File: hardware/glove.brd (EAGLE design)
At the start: 50.8 x 36.8 mm, 84 parts, among them J1 TC2030-JLINK-NL, J2 MICRO_USB_B_JST_MC5BR3-M404-4S, P1 DMP1045U, U1 NRF51822QF, U2 BNO055, U3 AT42QT1070, U4 MCP73831, U5 LP3855EMP-ADJ, X1 ABS05-32.768KHZ-9-T

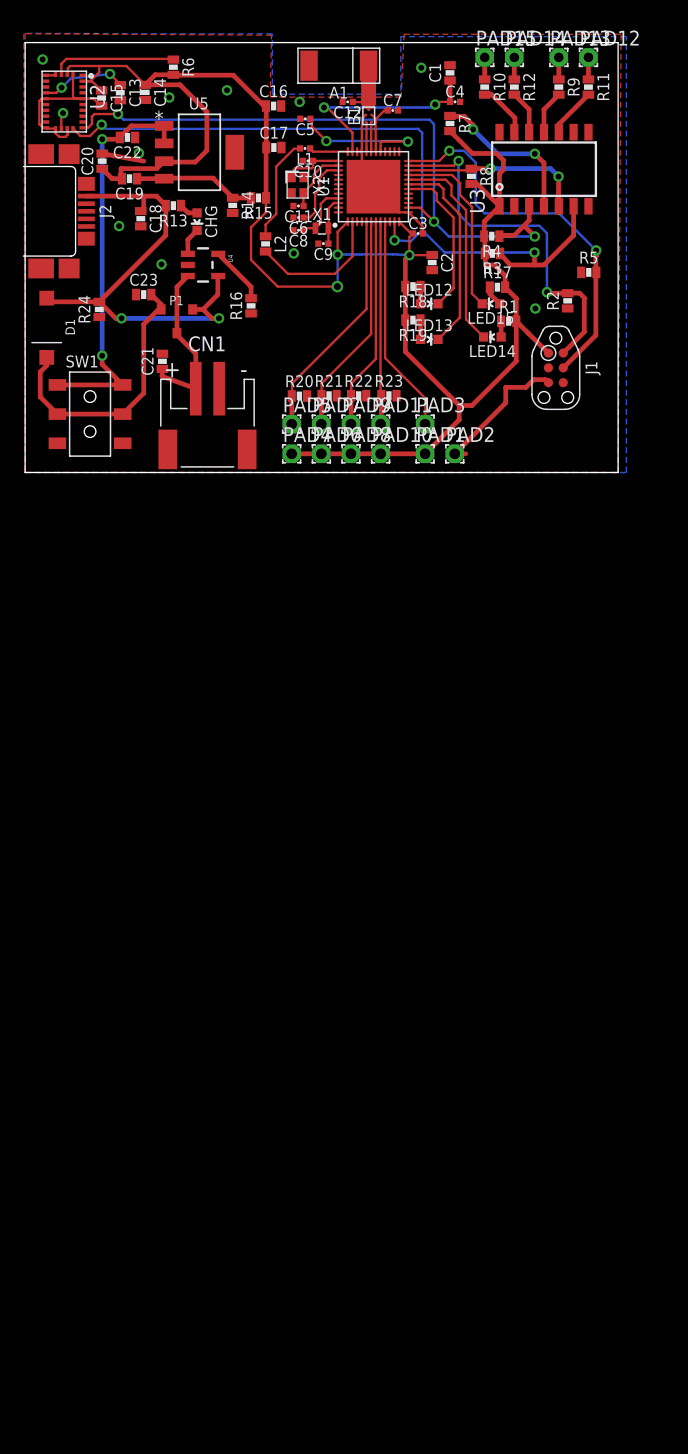
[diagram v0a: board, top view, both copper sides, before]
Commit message: Silkscreen/SPI LEDs
Cleaned up silk screen layer.
Added SPI connectors to schematic - still need to route.
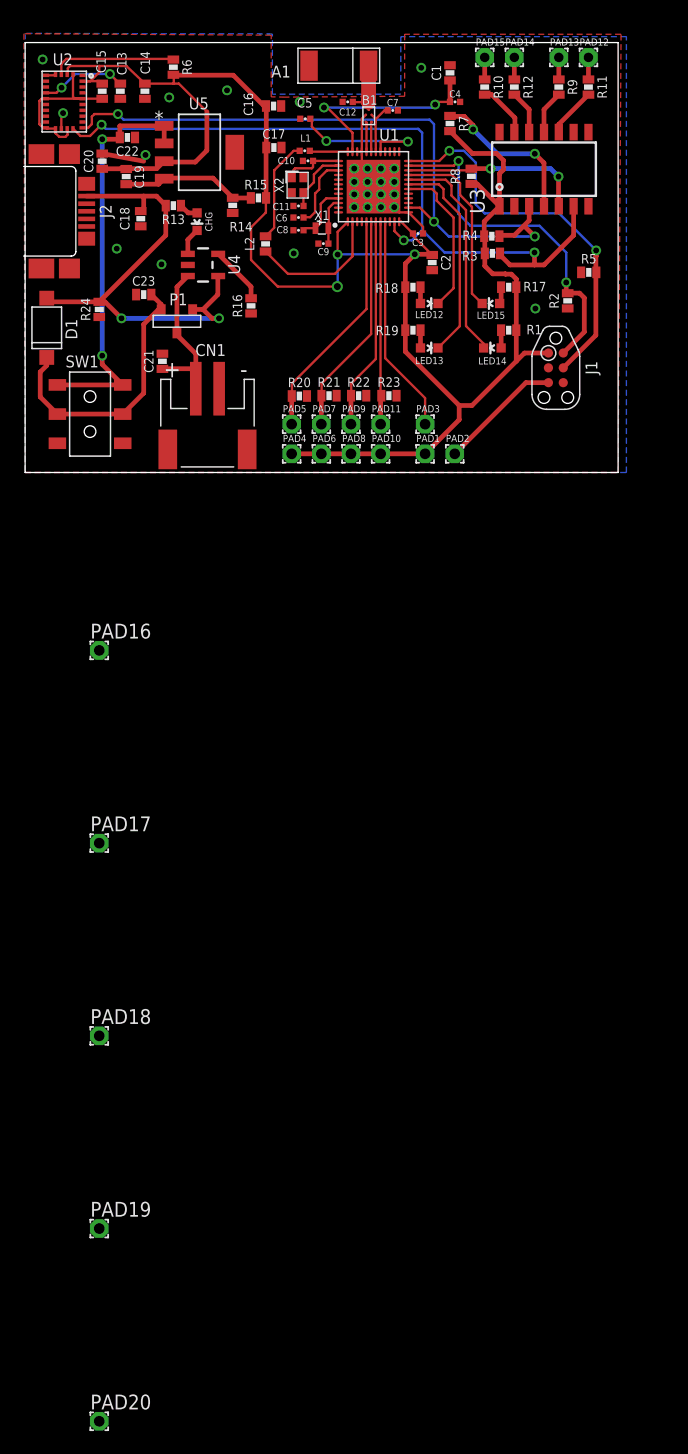
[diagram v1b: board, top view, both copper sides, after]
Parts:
- added PAD16, PAD17, PAD18, PAD19, PAD20: WIREPAD1,6/0,9, wirepad:1,6/0,9
- moved R17 0.97 mm to (41.4, 10.8)
- moved LED14 0.94 mm to (40.0, 5.59)
- moved R19 0.86 mm to (33.2, 7.11)
- moved R1 0.76 mm to (41.4, 7.11)
- moved LED13 0.74 mm to (34.6, 5.59)
- moved C15 0.59 mm to (6.60, 27.6)
- moved C19 0.33 mm to (8.66, 20.3), turned to 90 degrees
- moved L1 0.20 mm to (24.0, 22.5)
- moved C13 0.13 mm to (8.15, 27.6)
- moved C14 0.10 mm to (10.3, 27.6)
- moved R18 0.05 mm to (33.2, 10.8)
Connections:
- new net MISO: PAD19.1, U1.4
- new net MOSI: PAD20.1, U1.3
- new net SCLK: PAD18.1, U1.10
- net GND: now also PAD17.1
- net VCC: now also PAD16.1
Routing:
- net GND: track 45.7 -> 42.2 mm, vias 11 -> 27
- net VCC: track 154.9 -> 152.4 mm
- net N$7: track 10.5 -> 11.6 mm
- net N$19: track 31.2 -> 30.2 mm
- net N$6: track 18.0 -> 18.9 mm
- net N$41: track 14.5 -> 13.6 mm
- net N$43: track 17.4 -> 18.1 mm
- net N$5: track 34.9 -> 35.5 mm

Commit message: Added SPI LEDs to board
Need to fix clearance
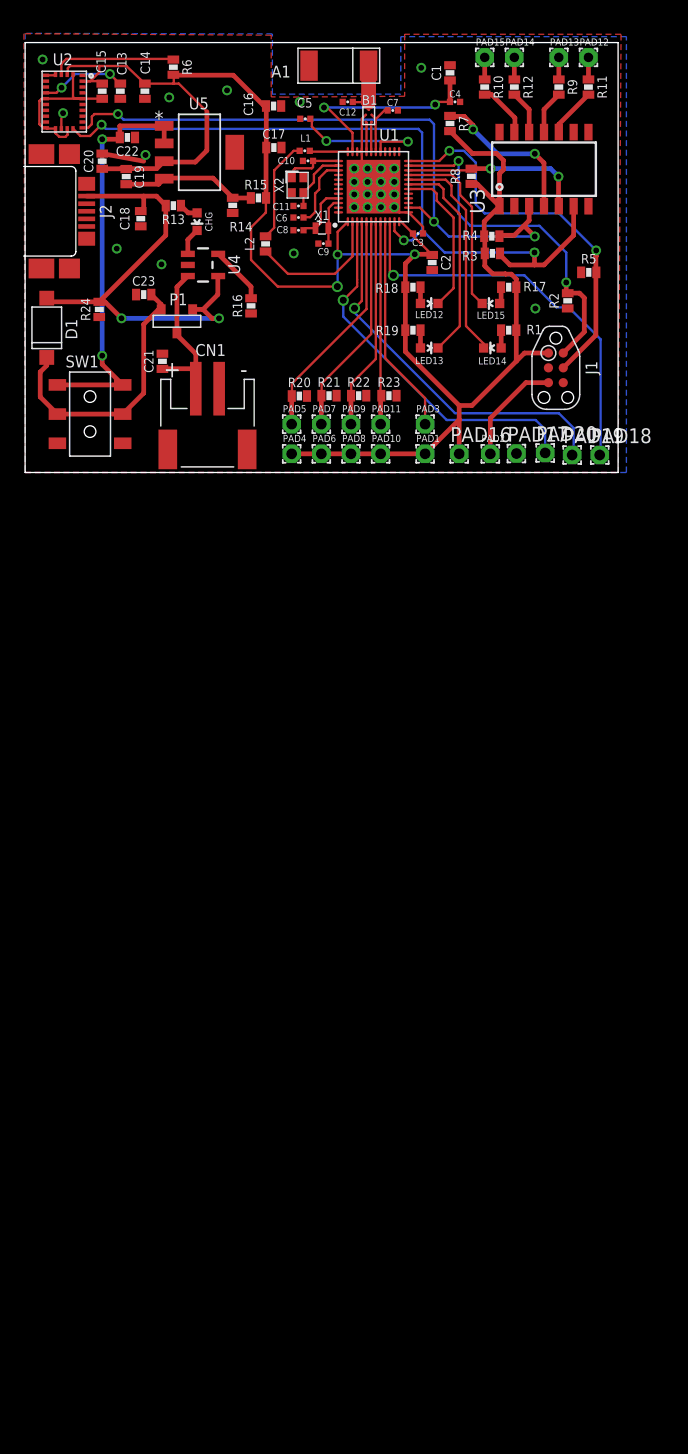
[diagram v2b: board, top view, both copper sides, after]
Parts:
- moved PAD20 91.3 mm to (44.6, -3.40)
- moved PAD19 77.7 mm to (46.9, -3.58)
- moved PAD18 65.7 mm to (49.2, -3.58)
- moved PAD17 48.9 mm to (42.1, -3.45)
- moved PAD16 35.1 mm to (37.2, -3.48)
- moved PAD2 3.05 mm to (39.9, -3.48)
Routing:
- net SCLK: track 0.00 -> 34.7 mm, vias 0 -> 1
- net MISO: track 0.00 -> 33.3 mm, vias 0 -> 1
- net MOSI: track 0.00 -> 31.9 mm, vias 0 -> 1
- net VCC: track 152.4 -> 155.5 mm
- net GND: track 42.2 -> 40.9 mm
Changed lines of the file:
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@@
 <?xml version="1.0" encoding="utf-8"?>
 <!DOCTYPE eagle SYSTEM "eagle.dtd">
-<eagle version="7.7.0">
+<eagle version="7.6.0">
 <drawing>
 <settings>
@@
 <attribute name="VALUE" x="30.4546" y="-0.3398" size="0.0254" layer="27"/>
 </element>
-<element name="PAD2" library="wirepad" package="1,6/0,9" value="WIREPAD1,6/0,9" x="36.8046" y="-3.4798" smashed="yes">
-<attribute name="NAME" x="36.0426" y="-2.4638" size="0.6096" layer="25" ratio="10"/>
-<attribute name="VALUE" x="36.8046" y="-2.8798" size="0.0254" layer="27"/>
+<element name="PAD2" library="wirepad" package="1,6/0,9" value="WIREPAD1,6/0,9" x="39.8526" y="-3.4798" smashed="yes">
+<attribute name="NAME" x="39.0906" y="-2.4638" size="0.6096" layer="25" ratio="10"/>
+<attribute name="VALUE" x="39.8526" y="-2.8798" size="0.0254" layer="27"/>
 </element>
 <element name="PAD3" library="wirepad" package="1,6/0,9" value="WIREPAD1,6/0,9" x="34.2646" y="-0.9398" smashed="yes">
@@
 <attribute name="VALUE" x="-1.3208" y="11.1252" size="1.27" layer="27" rot="R270"/>
 </element>
-<element name="PAD16" library="wirepad" package="1,6/0,9" value="WIREPAD1,6/0,9" x="6.35" y="-20.32"/>
-<element name="PAD17" library="wirepad" package="1,6/0,9" value="WIREPAD1,6/0,9" x="6.35" y="-36.83"/>
-<element name="PAD18" library="wirepad" package="1,6/0,9" value="WIREPAD1,6/0,9" x="6.35" y="-53.34"/>
-<element name="PAD19" library="wirepad" package="1,6/0,9" value="WIREPAD1,6/0,9" x="6.35" y="-69.85"/>
-<element name="PAD20" library="wirepad" package="1,6/0,9" value="WIREPAD1,6/0,9" x="6.35" y="-86.36"/>
+<element name="PAD16" library="wirepad" package="1,6/0,9" value="WIREPAD1,6/0,9" x="37.1856" y="-3.4798"/>
+<element name="PAD17" library="wirepad" package="1,6/0,9" value="WIREPAD1,6/0,9" x="42.0878" y="-3.4544"/>
+<element name="PAD18" library="wirepad" package="1,6/0,9" value="WIREPAD1,6/0,9" x="49.2252" y="-3.5814"/>
+<element name="PAD19" library="wirepad" package="1,6/0,9" value="WIREPAD1,6/0,9" x="46.863" y="-3.5814"/>
+<element name="PAD20" library="wirepad" package="1,6/0,9" value="WIREPAD1,6/0,9" x="44.5516" y="-3.4036"/>
 </elements>
 <signals>
@@
 <via x="33.9344" y="29.591" extent="1-16" drill="0.5"/>
 <via x="43.7134" y="8.9662" extent="1-16" drill="0.5"/>
-<wire x1="36.8046" y1="-3.4798" x2="42.9006" y2="2.6162" width="0.4064" layer="1"/>
 <wire x1="42.9006" y1="2.6162" x2="44.831" y2="2.6162" width="0.4064" layer="1"/>
 <via x="28.194" y="20.955" extent="1-16" drill="0.5"/>
@@
 <contactref element="PAD17" pad="1"/>
 <wire x1="6.593" y1="26.9454" x2="6.604" y2="26.9344" width="0.2032" layer="1"/>
-<wire x1="16.621" y1="2.0998" x2="6.35" y2="-36.83" width="0" layer="19" extent="1-1"/>
+<wire x1="39.8526" y1="-3.4798" x2="39.8526" y2="-0.4318" width="0.4064" layer="1"/>
+<wire x1="39.8526" y1="-0.4318" x2="42.9006" y2="2.6162" width="0.4064" layer="1"/>
 </signal>
 <signal name="N$14">
@@
 <wire x1="32.5732" y1="12.812" x2="33.3756" y2="13.6144" width="0.4064" layer="1"/>
 <contactref element="PAD16" pad="1"/>
-<wire x1="8.2146" y1="20.955" x2="11.2776" y2="20.955" width="0.4064" layer="1"/>
+<wire x1="8.2146" y1="20.955" x2="8.89" y2="20.955" width="0.4064" layer="1"/>
+<wire x1="8.89" y1="20.955" x2="11.2776" y2="20.955" width="0.4064" layer="1"/>
 <wire x1="11.2776" y1="20.955" x2="11.9126" y2="21.59" width="0.4064" layer="1"/>
 <wire x1="6.604" y1="20.94" x2="8.6406" y2="20.94" width="0.4064" layer="1"/>
@@
 <wire x1="40.0558" y1="11.938" x2="41.133" y2="11.938" width="0.4064" layer="1"/>
 <wire x1="41.133" y1="11.938" x2="41.1584" y2="11.9126" width="0.4064" layer="1"/>
-<wire x1="8.2146" y1="20.955" x2="8.6406" y2="20.94" width="0" layer="19" extent="1-1"/>
-<wire x1="6.35" y1="-20.32" x2="22.6314" y2="-3.4798" width="0" layer="19" extent="1-1"/>
+<wire x1="37.1856" y1="-3.4798" x2="37.1856" y2="-0.5588" width="0.4064" layer="1"/>
+<wire x1="8.6406" y1="20.94" x2="8.875" y2="20.94" width="0.2032" layer="1"/>
+<wire x1="8.875" y1="20.94" x2="8.89" y2="20.955" width="0.2032" layer="1"/>
 </signal>
 <signal name="N$19">
@@
 <contactref element="U1" pad="4"/>
 <contactref element="PAD19" pad="1"/>
-<wire x1="28.845" y1="16.4056" x2="6.35" y2="-69.85" width="0" layer="19" extent="1-1"/>
+<wire x1="28.845" y1="16.4056" x2="28.845" y2="9.6172" width="0.2032" layer="1"/>
+<wire x1="28.845" y1="9.6172" x2="28.2194" y2="8.9916" width="0.2032" layer="1"/>
+<via x="28.2194" y="8.9916" extent="1-16" drill="0.6"/>
+<wire x1="28.2194" y1="8.9916" x2="28.2194" y2="8.6106" width="0.2032" layer="16"/>
+<wire x1="28.2194" y1="8.6106" x2="36.83" y2="0" width="0.2032" layer="16"/>
+<wire x1="36.83" y1="0" x2="45.72" y2="0" width="0.2032" layer="16"/>
+<wire x1="45.72" y1="0" x2="46.99" y2="-1.27" width="0.2032" layer="16"/>
+<wire x1="46.99" y1="-1.27" x2="46.99" y2="-3.4544" width="0.2032" layer="16"/>
+<wire x1="46.863" y1="-3.5814" x2="46.99" y2="-3.4544" width="0.2032" layer="16"/>
 </signal>
 <signal name="MOSI">
 <contactref element="U1" pad="3"/>
 <contactref element="PAD20" pad="1"/>
-<wire x1="28.445" y1="16.4056" x2="6.35" y2="-86.36" width="0" layer="19" extent="1-1"/>
+<wire x1="28.445" y1="16.4056" x2="28.445" y2="11.43" width="0.2032" layer="1"/>
+<wire x1="28.445" y1="11.43" x2="28.445" y2="11.173" width="0.2032" layer="1"/>
+<wire x1="27.2542" y1="9.6774" x2="27.2542" y2="8.2804" width="0.2032" layer="16"/>
+<wire x1="27.2542" y1="8.2804" x2="36.1188" y2="-0.5842" width="0.2032" layer="16"/>
+<wire x1="36.1188" y1="-0.5842" x2="43.7388" y2="-0.5842" width="0.2032" layer="16"/>
+<wire x1="43.7388" y1="-0.5842" x2="44.5516" y2="-1.397" width="0.2032" layer="16"/>
+<via x="27.2542" y="9.6774" extent="1-16" drill="0.6"/>
+<wire x1="27.2542" y1="9.6774" x2="28.445" y2="10.8682" width="0.2032" layer="1"/>
+<wire x1="28.445" y1="10.8682" x2="28.445" y2="11.173" width="0.2032" layer="1"/>
+<wire x1="44.5516" y1="-3.4036" x2="44.5516" y2="-1.397" width="0.2032" layer="16"/>
 </signal>
 <signal name="SCLK">
 <contactref element="U1" pad="10"/>
 <contactref element="PAD18" pad="1"/>
-<wire x1="31.245" y1="16.4056" x2="6.35" y2="-53.34" width="0" layer="19" extent="1-1"/>
+<wire x1="31.245" y1="16.4056" x2="31.245" y2="12.1128" width="0.2032" layer="1"/>
+<wire x1="31.245" y1="12.1128" x2="31.5468" y2="11.811" width="0.2032" layer="1"/>
+<via x="31.5468" y="11.811" extent="1-16" drill="0.6"/>
+<wire x1="31.5468" y1="11.811" x2="42.7736" y2="11.811" width="0.2032" layer="16"/>
+<wire x1="42.7736" y1="11.811" x2="45.5168" y2="9.0678" width="0.2032" layer="16"/>
+<wire x1="45.5168" y1="9.0678" x2="46.5582" y2="9.0678" width="0.2032" layer="16"/>
+<wire x1="46.5582" y1="9.0678" x2="49.3014" y2="6.3246" width="0.2032" layer="16"/>
+<wire x1="49.3014" y1="6.3246" x2="49.3014" y2="-3.5052" width="0.2032" layer="16"/>
+<wire x1="49.3014" y1="-3.5052" x2="49.2252" y2="-3.5814" width="0.2032" layer="16"/>
 </signal>
 </signals>

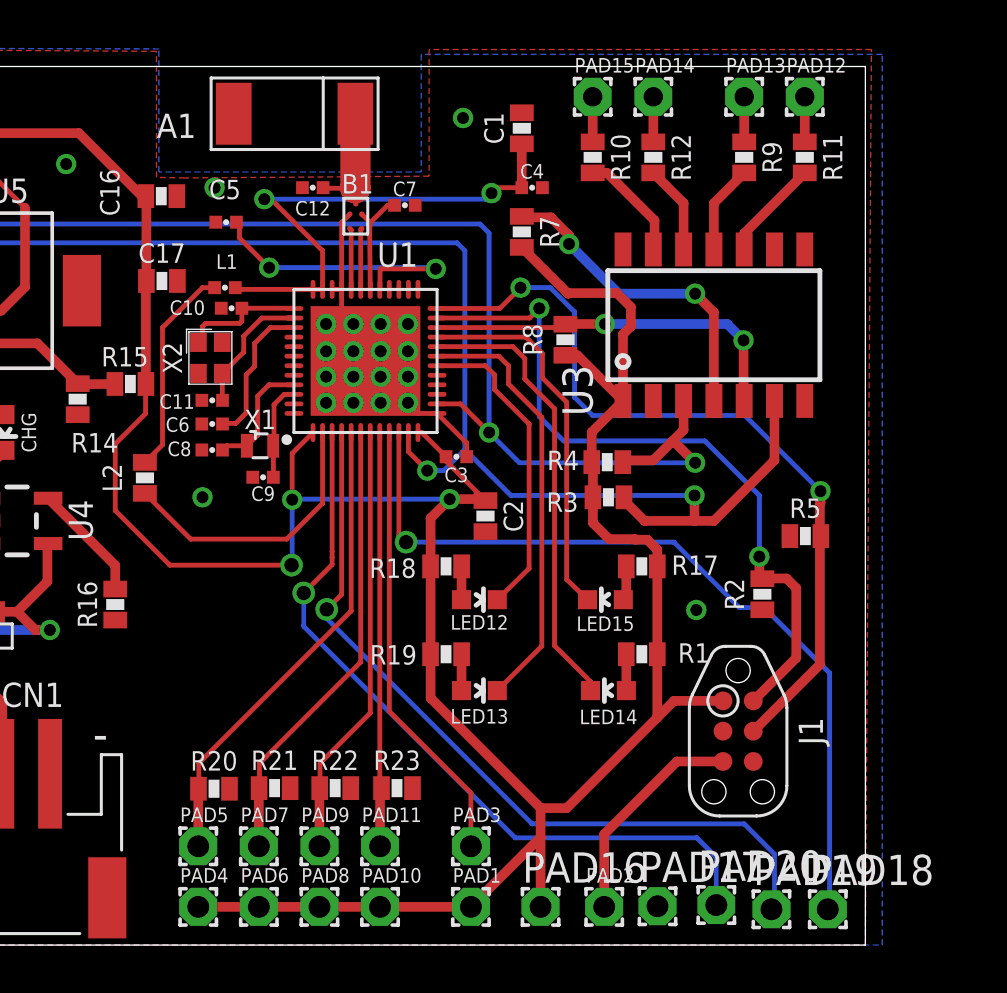
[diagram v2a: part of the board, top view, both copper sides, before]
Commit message: Adjusted Silkscreen
Named and adjusted pads and added slikscreen text
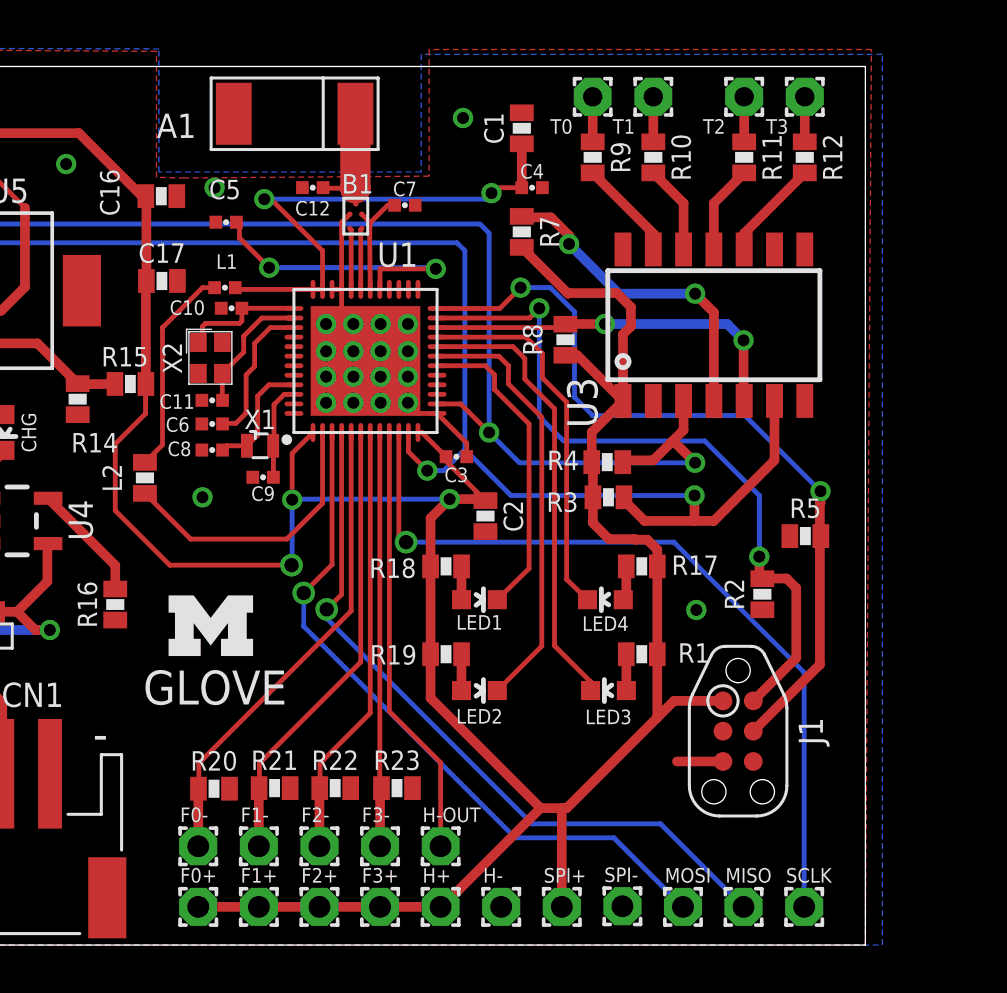
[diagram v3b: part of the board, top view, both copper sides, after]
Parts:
- removed PAD1, PAD16, PAD17, PAD18, PAD19, PAD2, PAD20, PAD3: WIREPAD1,6/0,9, wirepad:1,6/0,9
- added H+, H-, H-OUT, MISO, MOSI, SCLK, SPI+, SPI-: WIREPAD1,6/0,9, wirepad:1,6/0,9
- added U$1: (no value), logos:UMICH_SOLID_100MIL
- moved R12 6.35 mm to (48.3, 27.9)
- moved R9 6.35 mm to (39.4, 27.9)
- moved R10 2.54 mm to (41.9, 27.9)
- moved R11 2.54 mm to (45.7, 27.9)
- renumbered LED12 to LED1, LED13 to LED2, LED14 to LED3, LED15 to LED4, PAD10 to F3+, PAD11 to F3-, PAD12 to T3, PAD13 to T2, PAD14 to T1, PAD15 to T0, PAD4 to F0+, PAD5 to F0-, PAD6 to F1+, PAD7 to F1-, PAD8 to F2+, PAD9 to F2-
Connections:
- net GND: now also H-.1, SPI-.1; no longer PAD17.1, PAD2.1
- net HEART: now also H-OUT.1; no longer PAD3.1
- net MISO: now also MISO.1; no longer PAD19.1
- net MOSI: now also MOSI.1; no longer PAD20.1
- net N$31: now also R12.2; no longer R11.2
- net N$32: now also R12.1; no longer R11.1
- net N$33: now also R11.2; no longer R9.2
- net N$34: now also R11.1; no longer R9.1
- net N$35: now also R10.2; no longer R12.2
- net N$36: now also R10.1; no longer R12.1
- net N$37: now also R9.2; no longer R10.2
- net N$39: now also R9.1; no longer R10.1
- net SCLK: now also SCLK.1; no longer PAD18.1
- net VCC: now also H+.1, SPI+.1; no longer PAD1.1, PAD16.1
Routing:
- net GND: track 40.9 -> 33.6 mm
- net MISO: track 33.3 -> 30.5 mm
- net MOSI: track 31.9 -> 29.4 mm
- net SCLK: track 34.7 -> 33.5 mm
- net HEART: track 18.8 -> 18.2 mm
- net VCC: track 155.5 -> 156.1 mm
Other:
- board text added: "EECS 473 F16 - Team GLOVE Nick Bertoldi Ben Heckathorn Ryan O'Keefe Adrian Padin Tim Schumacher"
- board text added: "GLOVE"
